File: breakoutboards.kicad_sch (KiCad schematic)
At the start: 18 parts, among them J13 USB_A, J15 Conn_01x16, J16 Conn_01x16, J3 Conn_01x12, J4 Conn_01x12, J5 USB_C_Receptacle_USB2.0_16P, U3 AMS1117-3.3

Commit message: 1.4.1 schematic update
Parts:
- I2C-2: value Conn_01x04_Female -> ~; symbol Connector:Conn_01x04_Female -> Connector:Conn_01x04_Socket
- I2C-3: symbol Connector:Conn_01x04_Female -> Connector:Conn_01x04_Socket
- J13: footprint USB-vertical-jlcpcb:USB-A-TH_UBAS-4R-D14D-4D-LF-SN -> usb-female:USB-A-TH_USB-2.0-A-F-180-JCJ-H20.5
- SPI-1: symbol Connector:Conn_01x06_Female -> Connector:Conn_01x06_Socket
- pwr5v1: symbol Connector:Conn_01x02_Female -> Connector:Conn_01x02_Socket
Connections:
- net +5V: now also pwr5v1.2 (Pin_2); no longer pwr5v1.1 (Pin_1)
- net GND: now also pwr5v1.1 (Pin_1); no longer pwr5v1.2 (Pin_2)
- net DC-read-stage2: now reaches J3.5 (Pin_5), J4.5 (Pin_5)
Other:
- note added: "*Use input_pullup* invert logic [not input]"
- note added: "The I2C bus connection is used by the ADE7953, but here are 2 more that add more extensibility to the board as a whole. One of these will may be used by a PN532 RFID Card Reader. --- NOTE: Cut jumpers & solder in THT resistors if you find the I2C data has a bad rise-time/ connection."
- note added: "https://learn.adafruit.com/ adafruit-wiz5500-wiznet- ethernet-featherwing/pinouts <--IRQ (also maybe not needed)"
- note removed: "The I2C bus connection is used by the ADE7953, but here are 2 more that add more extensibility to the board as a whole. One of these will likely be used by a PN532 RFID Card Reader."
- note removed: "eth-wng-irq"
- note removed: "https://learn.adafruit.com/ adafruit-wiz5500-wiznet- ethernet-featherwing/pinouts ------>"
- moved on the sheet: JP17, JP18, JP19, R32, R33, R7, R8, U3, pwr5v1

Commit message: update reference values for better ibom
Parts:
- J11: renamed from I2C-2; value ~ -> Conn_01x04_Female
- J17: renamed from pwr5v1; value extra -> Conn_01x02_Female; now not fitted
- renumbered J3 to J1, I2C-3 to J12, SPI-1 to J16, J16 to J2, J4 to J3, J15 to J4, J5 to J8, J13 to J9
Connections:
- net GND: now also J9.6 (Shield)
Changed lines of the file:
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@@
 	(title_block
 		(title "Breakout Connections & Power")
-		(date "2022-10-09")
-		(rev "3")
+		(date "2025-09-25")
+		(rev "4")
 		(company "Corey Rice & MakeHaven")
 		(comment 1 "Breakouts for I2C and SPI communication with external boards.")
@@
 	)
 	(junction
+		(at 143.51 100.33)
+		(diameter 0)
+		(color 0 0 0 0)
+	)
+	(junction
 		(at 60.96 149.86)
 		(diameter 0)
@@
 	(wire
 		(pts
+			(xy 140.97 99.06) (xy 140.97 100.33)
+		)
+		(stroke
+			(width 0)
+			(type default)
+		)
+	)
+	(wire
+		(pts
 			(xy 116.84 162.56) (xy 125.73 162.56)
 		)
@@
 	(wire
 		(pts
+			(xy 140.97 100.33) (xy 143.51 100.33)
+		)
+		(stroke
+			(width 0)
+			(type default)
+		)
+	)
+	(wire
+		(pts
 			(xy 57.15 142.24) (xy 60.96 142.24)
 		)
@@
 		(dnp no)
 		(fields_autoplaced yes)
-		(property "Reference" "J5"
+		(property "Reference" "J8"
 			(at 172.72 57.15 0)
 			(effects
@@
 			(project "wing-combo"
 				(path "/586efc0f-7de2-49a7-ac21-ecfef2f716d6/3f0e9b91-fe15-47d5-84d6-aa71b368b91e/76df30f3-bf0f-4a81-9e12-488966ab08bf"
-					(reference "J5")
+					(reference "J8")
 					(unit 1)
 				)
@@
 		(dnp no)
 		(fields_autoplaced yes)
-		(property "Reference" "J13"
+		(property "Reference" "J9"
 			(at 146.05 76.2 0)
 			(effects
@@
 		(pin "5"
 		)
+		(pin "6"
+		)
 		(instances
 			(project "wing-combo"
 				(path "/586efc0f-7de2-49a7-ac21-ecfef2f716d6/3f0e9b91-fe15-47d5-84d6-aa71b368b91e/76df30f3-bf0f-4a81-9e12-488966ab08bf"
-					(reference "J13")
+					(reference "J9")
 					(unit 1)
 				)
@@
 		(on_board yes)
 		(dnp no)
-		(property "Reference" "SPI-1"
+		(property "Reference" "J16"
 			(at 244.856 77.216 0)
 			(effects
@@
 			(project "wing-combo"
 				(path "/586efc0f-7de2-49a7-ac21-ecfef2f716d6/3f0e9b91-fe15-47d5-84d6-aa71b368b91e/76df30f3-bf0f-4a81-9e12-488966ab08bf"
-					(reference "SPI-1")
+					(reference "J16")
 					(unit 1)
 				)
@@
 		(on_board yes)
 		(dnp no)
-		(property "Reference" "J3"
+		(property "Reference" "J1"
 			(at 64.77 129.54 0)
 			(effects
@@
 			(project "wing-combo"
 				(path "/586efc0f-7de2-49a7-ac21-ecfef2f716d6/3f0e9b91-fe15-47d5-84d6-aa71b368b91e/76df30f3-bf0f-4a81-9e12-488966ab08bf"
-					(reference "J3")
+					(reference "J1")
 					(unit 1)
 				)
@@
 		(on_board yes)
 		(dnp yes)
-		(property "Reference" "J4"
+		(property "Reference" "J3"
 			(at 72.39 129.54 0)
 			(effects
@@
 			(project "wing-combo"
 				(path "/586efc0f-7de2-49a7-ac21-ecfef2f716d6/3f0e9b91-fe15-47d5-84d6-aa71b368b91e/76df30f3-bf0f-4a81-9e12-488966ab08bf"
-					(reference "J4")
+					(reference "J3")
 					(unit 1)
 				)
@@
 		(on_board yes)
 		(dnp no)
-		(property "Reference" "J16"
+		(property "Reference" "J2"
 			(at 113.538 129.54 0)
 			(effects
@@
 			(project "wing-combo"
 				(path "/586efc0f-7de2-49a7-ac21-ecfef2f716d6/3f0e9b91-fe15-47d5-84d6-aa71b368b91e/76df30f3-bf0f-4a81-9e12-488966ab08bf"
-					(reference "J16")
+					(reference "J2")
 					(unit 1)
 				)
@@
 		(on_board yes)
 		(dnp no)
-		(property "Reference" "I2C-2"
+		(property "Reference" "J11"
 			(at 64.77 88.9 0)
 			(effects
@@
 			)
 		)
-		(property "Value" "~"
+		(property "Value" "Conn_01x04_Female"
 			(at 64.77 86.36 0)
 			(effects
@@
 			(project "wing-combo"
 				(path "/586efc0f-7de2-49a7-ac21-ecfef2f716d6/3f0e9b91-fe15-47d5-84d6-aa71b368b91e/76df30f3-bf0f-4a81-9e12-488966ab08bf"
-					(reference "I2C-2")
+					(reference "J11")
 					(unit 1)
 				)
@@
 		(in_bom no)
 		(on_board yes)
-		(dnp no)
-		(property "Reference" "pwr5v1"
+		(dnp yes)
+		(property "Reference" "J17"
 			(at 130.81 88.9001 0)
 			(effects
@@
 			)
 		)
-		(property "Value" "extra"
+		(property "Value" "Conn_01x02_Female"
 			(at 130.81 86.3601 0)
 			(effects
@@
 				)
 				(justify left)
+				(hide yes)
 			)
 		)
@@
 			(project "wing-combo"
 				(path "/586efc0f-7de2-49a7-ac21-ecfef2f716d6/3f0e9b91-fe15-47d5-84d6-aa71b368b91e/76df30f3-bf0f-4a81-9e12-488966ab08bf"
-					(reference "pwr5v1")
+					(reference "J17")
 					(unit 1)
 				)
@@
 		(on_board yes)
 		(dnp no)
-		(property "Reference" "I2C-3"
+		(property "Reference" "J12"
 			(at 92.71 88.9 0)
 			(effects
@@
 			(project "wing-combo"
 				(path "/586efc0f-7de2-49a7-ac21-ecfef2f716d6/3f0e9b91-fe15-47d5-84d6-aa71b368b91e/76df30f3-bf0f-4a81-9e12-488966ab08bf"
-					(reference "I2C-3")
+					(reference "J12")
 					(unit 1)
 				)
@@
 		(on_board yes)
 		(dnp yes)
-		(property "Reference" "J15"
+		(property "Reference" "J4"
 			(at 105.918 129.54 0)
 			(effects
@@
 			(project "wing-combo"
 				(path "/586efc0f-7de2-49a7-ac21-ecfef2f716d6/3f0e9b91-fe15-47d5-84d6-aa71b368b91e/76df30f3-bf0f-4a81-9e12-488966ab08bf"
-					(reference "J15")
+					(reference "J4")
 					(unit 1)
 				)

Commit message: before new branch
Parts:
- removed JP17: no-filter-1, Jumper:SolderJumper-2_P1.3mm_Open_RoundedPad1.0x1.5mm, symbol Jumper:SolderJumper_2_Open
- added JP17: bridged, Jumper:SolderJumper-2_P1.3mm_Bridged_RoundedPad1.0x1.5mm, symbol Jumper:SolderJumper_2_Bridged
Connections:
- net +5V: now also JP17.2 (B)
- net at J1.10 (Pin_10), J3.10 (Pin_10): now also JP17.1 (A)
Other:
- note added: ">[!NOTE] The Feather will be powered by the onboard AC/DC power supply on the Wing by default. That means: > NEVER plug your computer's USB port into the Feather while the Wing is powered from the AC/DC power supply! > This woud backpower your Computer's USB and can cause serious harm to the computer. > > Here is what you should do: > 1. Program the Feather over USB (first time only) while it is 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"
- note removed: "If you solder-jumper JP17 (not advised): This board would be back-powering the USB. For that reason, it is advised that you do not have it conencted to your computer's USB port and wall-power at the same time. There is a real risk of damage to the computer. https://learn.adafruit.com/adafruit-huzzah32-esp32-feather/power-management#alternative-power-options-3122391 In that case: 1. Program the Fe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"

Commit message: nearly ready
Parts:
- removed J17: Conn_01x02_Female, Connector_PinHeader_2.54mm:PinHeader_1x02_P2.54mm_Vertical, symbol Connector:Conn_01x02_Socket
- removed J8: USB_C_Receptacle_USB2.0_16P, usbc:USB-C-TH_GT-USB-7055, symbol Connector:USB_C_Receptacle_USB2.0_16P
- removed J9: USB_A, usb-female:USB-A-TH_USB-2.0-A-F-180-JCJ-H20.5, symbol Connector:USB_A
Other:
- note removed: "Power-only USB out"
- note removed: "The Feather is powered via USB, by specification. These allow for short cables to supply 5V power. May be also used to power secondary microcontrollers (like for e-Ink)."

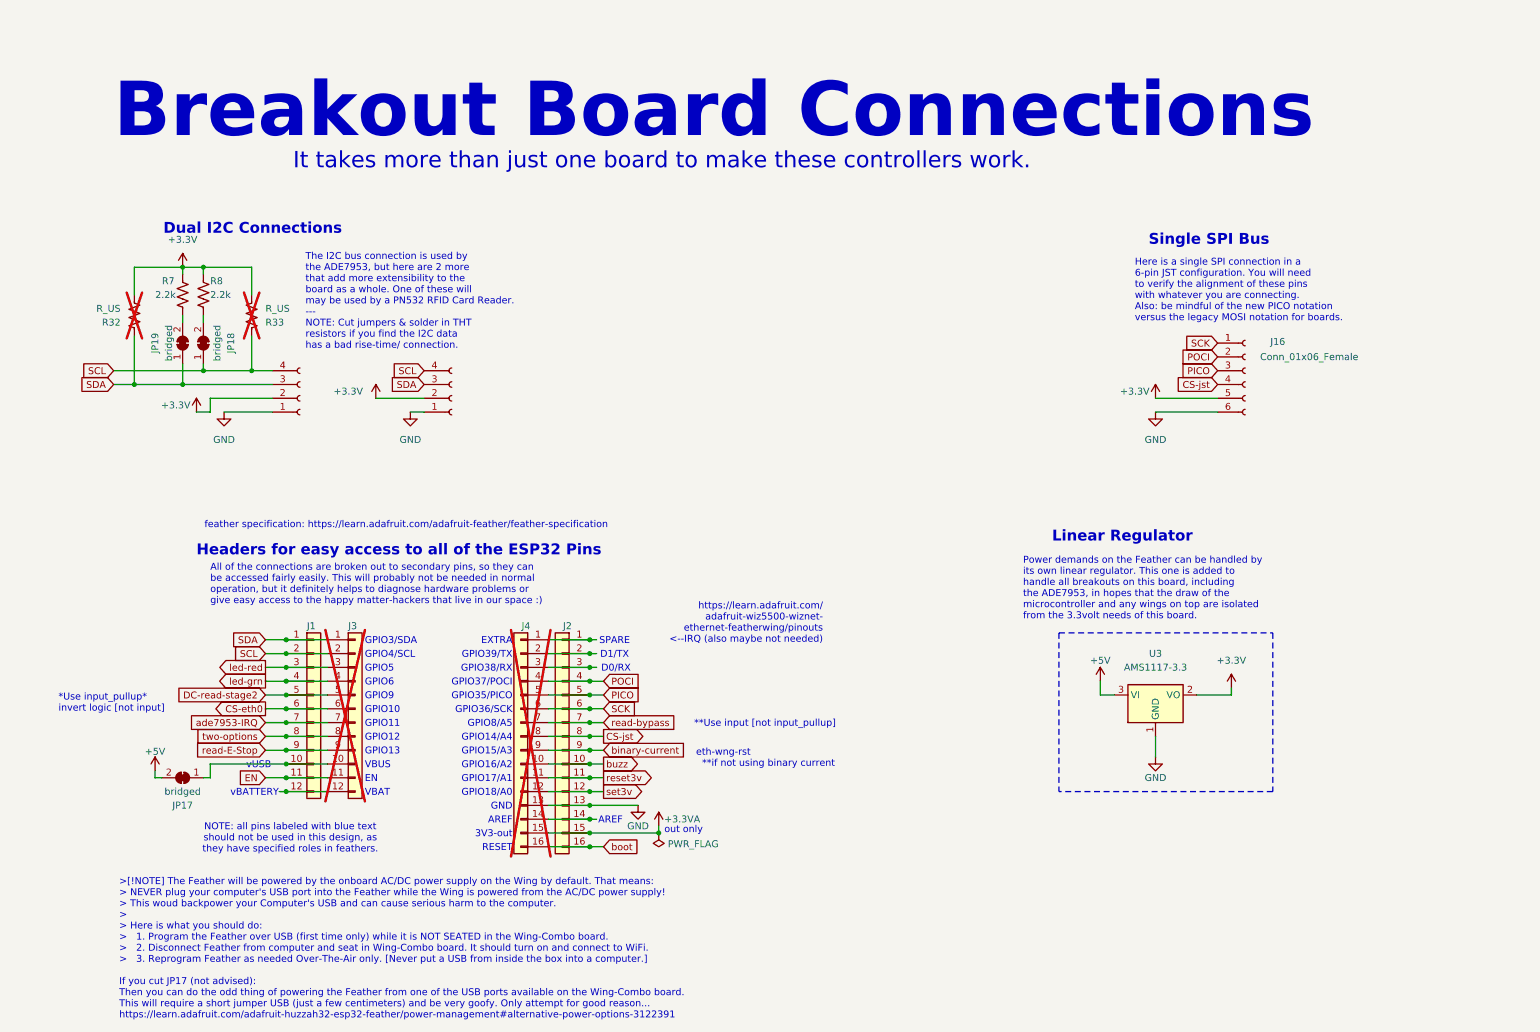
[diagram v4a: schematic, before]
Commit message: 5v binary current and cleanup
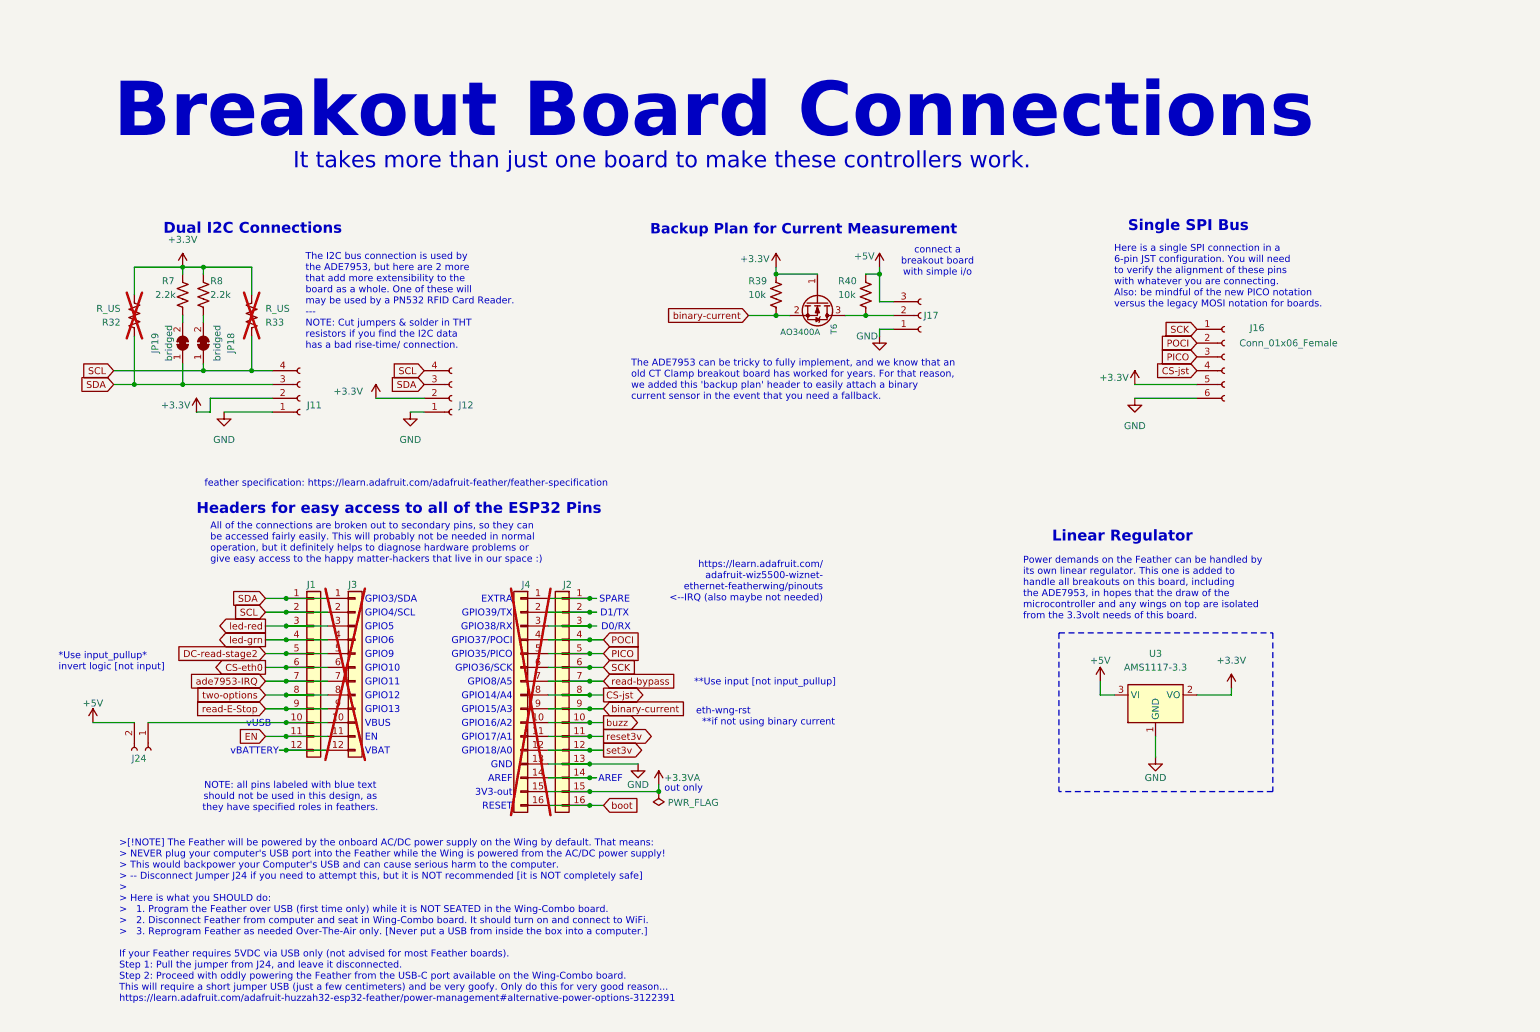
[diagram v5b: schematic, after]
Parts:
- removed JP17: bridged, Jumper:SolderJumper-2_P1.3mm_Bridged_RoundedPad1.0x1.5mm, symbol Jumper:SolderJumper_2_Bridged
- added J17: Conn_01x03_Female, Connector_JST:JST_PH_B3B-PH-K_1x03_P2.00mm_Vertical, symbol Connector:Conn_01x03_Socket
- added J24: powered, Connector_PinHeader_2.54mm:PinHeader_1x02_P2.54mm_Vertical, symbol Connector:Conn_01x02_Socket
- added R39, R40: 10k, Resistor_SMD:R_0603_1608Metric, symbol Device:R_US
- added T6: AO3400A, Package_TO_SOT_SMD:SOT-23, symbol Transistor_FET:AO3400A
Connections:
- net +3.3V: now also R39.2, T6.1 (G)
- net +5V: now also J17.3 (Pin_3), J24.2 (Pin_2), R40.2
- net GND: now also J17.1 (Pin_1)
- net binary-current: now also R39.1, T6.2 (S)
- net at J1.10 (Pin_10), J3.10 (Pin_10): now also J24.1 (Pin_1)
- new net: J17.2 (Pin_2), R40.1, T6.3 (D)
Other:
- note added: ">[!NOTE] The Feather will be powered by the onboard AC/DC power supply on the Wing by default. That means: > NEVER plug your computer's USB port into the Feather while the Wing is powered from the AC/DC power supply! > This would backpower your Computer's USB and can cause serious harm to the computer. > -- Disconnect Jumper J24 if you need to attempt this, but it is NOT recommended [it is NOT co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"
- note added: "Backup Plan for Current Measurement"
- note added: "The ADE7953 can be tricky to fully implement, and we know that an old CT Clamp breakout board has worked for years. For that reason, we added this 'backup plan' header to easily attach a binary current sensor in the event that you need a fallback."
- note added: "connect a breakout board with simple i/o"
- note removed: ">[!NOTE] The Feather will be powered by the onboard AC/DC power supply on the Wing by default. That means: > NEVER plug your computer's USB port into the Feather while the Wing is powered from the AC/DC power supply! > This woud backpower your Computer's USB and can cause serious harm to the computer. > > Here is what you should do: > 1. Program the Feather over USB (first time only) while it is 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"
- moved on the sheet: J1, J16, J2, J3, J4

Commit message: close enough for 3D export
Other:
- note added: "**Technically, this is just a spare level-shifted GPIO input you can use."
- note added: "5VDC"
- note added: "<--not used"
- note added: "For the M3050, you connect: - K2 to J17-Pin_1 (GND) - K1 to J17-Pin_2 (Signal) - Do not connect J17-Pin_3 This AC Current Switch simply connects signal to ground and gets powered by the AC current it observes. Invert your logic."
- note added: "M3050 Current Sensing Switch"
- note added: "Signal"
- note added: "The ADE7953 can be tricky to fully implement, and we know that an old CT Clamp breakout board has worked for years. For that reason, we added this flexible 'backup plan' to easily attach an AC current switch or breakout board (with digital out) if you need a fallback. [!WARNING] Use an AC current sensor here, with digital output (NOT Analog) or this will not work. Try this:"
- note added: "The three-pin connector is there for flexibility. We don't use all 3. But you could if you found some awesome sensor that needed 5v to run and output digital signals."
- note added: "U d d d"
- note added: "Use AC Current Sensing Switch"
- note removed: "The ADE7953 can be tricky to fully implement, and we know that an old CT Clamp breakout board has worked for years. For that reason, we added this 'backup plan' header to easily attach a binary current sensor in the event that you need a fallback."
- note removed: "connect a breakout board with simple i/o"
- moved on the sheet: J11, J12, J16, J17, JP18, JP19, R32, R33, R39, R40, R7, R8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
